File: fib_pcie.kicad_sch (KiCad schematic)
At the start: 59 parts, among them J901 Bus_M.2_2199230-6, J902 Bus_M.2_1-2199230-6, Y901 Oscillator_SMD_32.768kHz_ECS_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

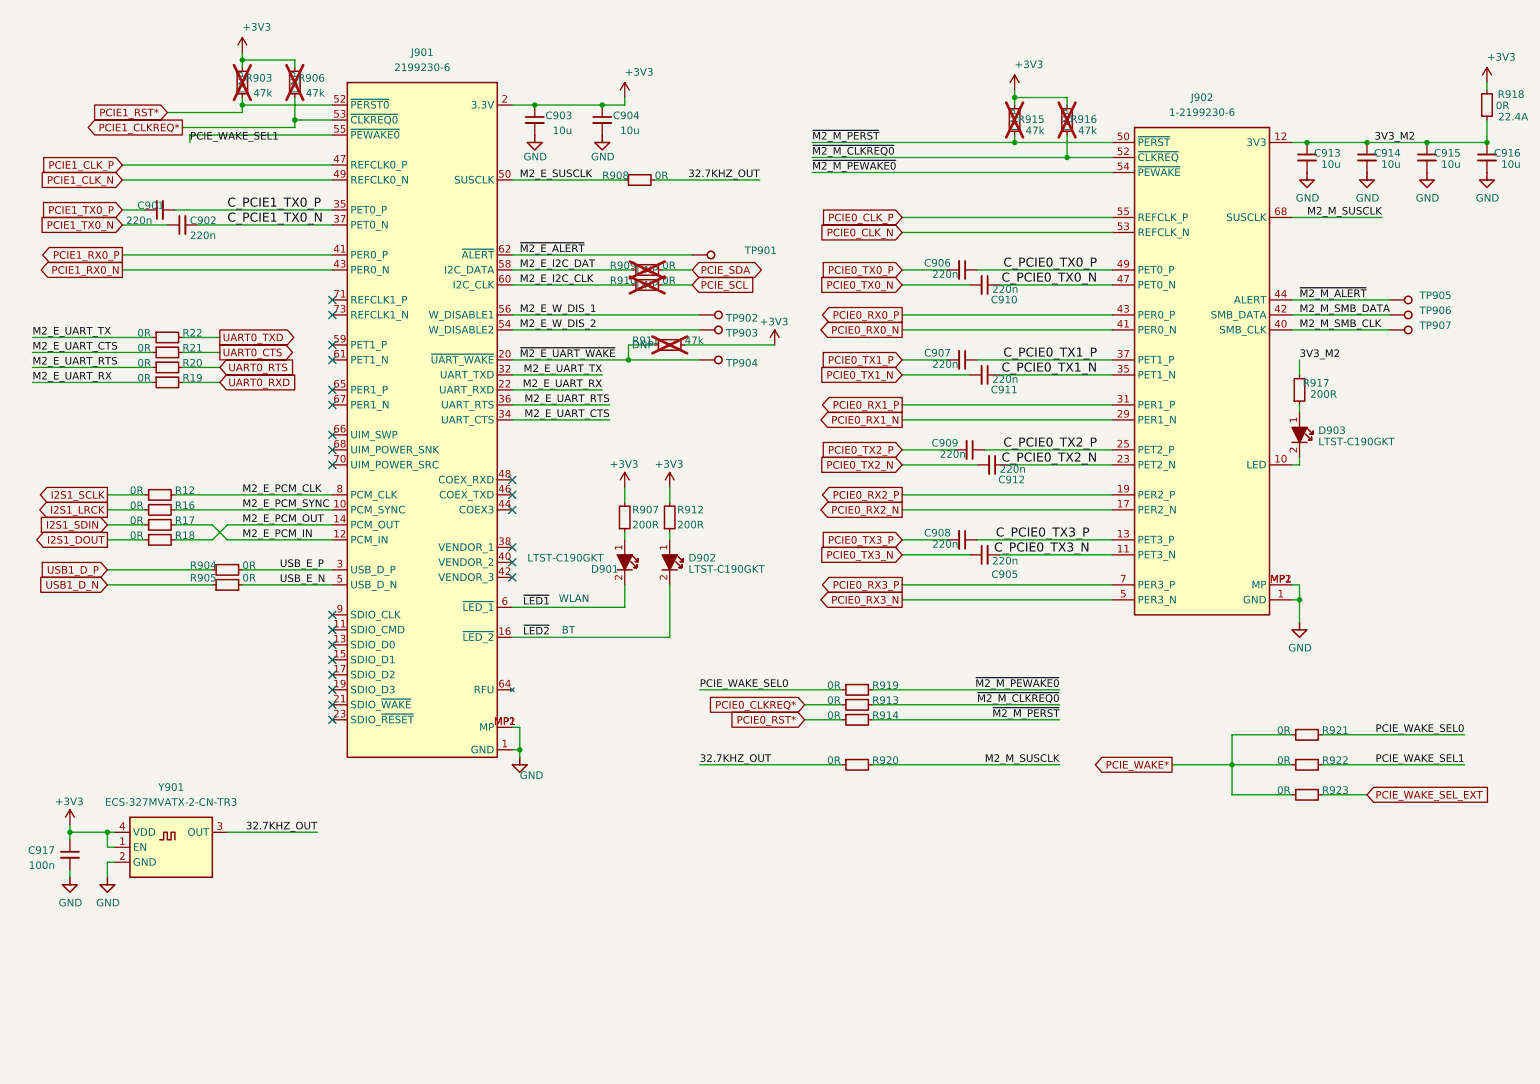
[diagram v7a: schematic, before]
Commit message: added all missing footprints, fixed library & footprint links, did layout out 99% of components, all that's left is rtc(?), peripherals, routing & lengthmatching and final sanity checks
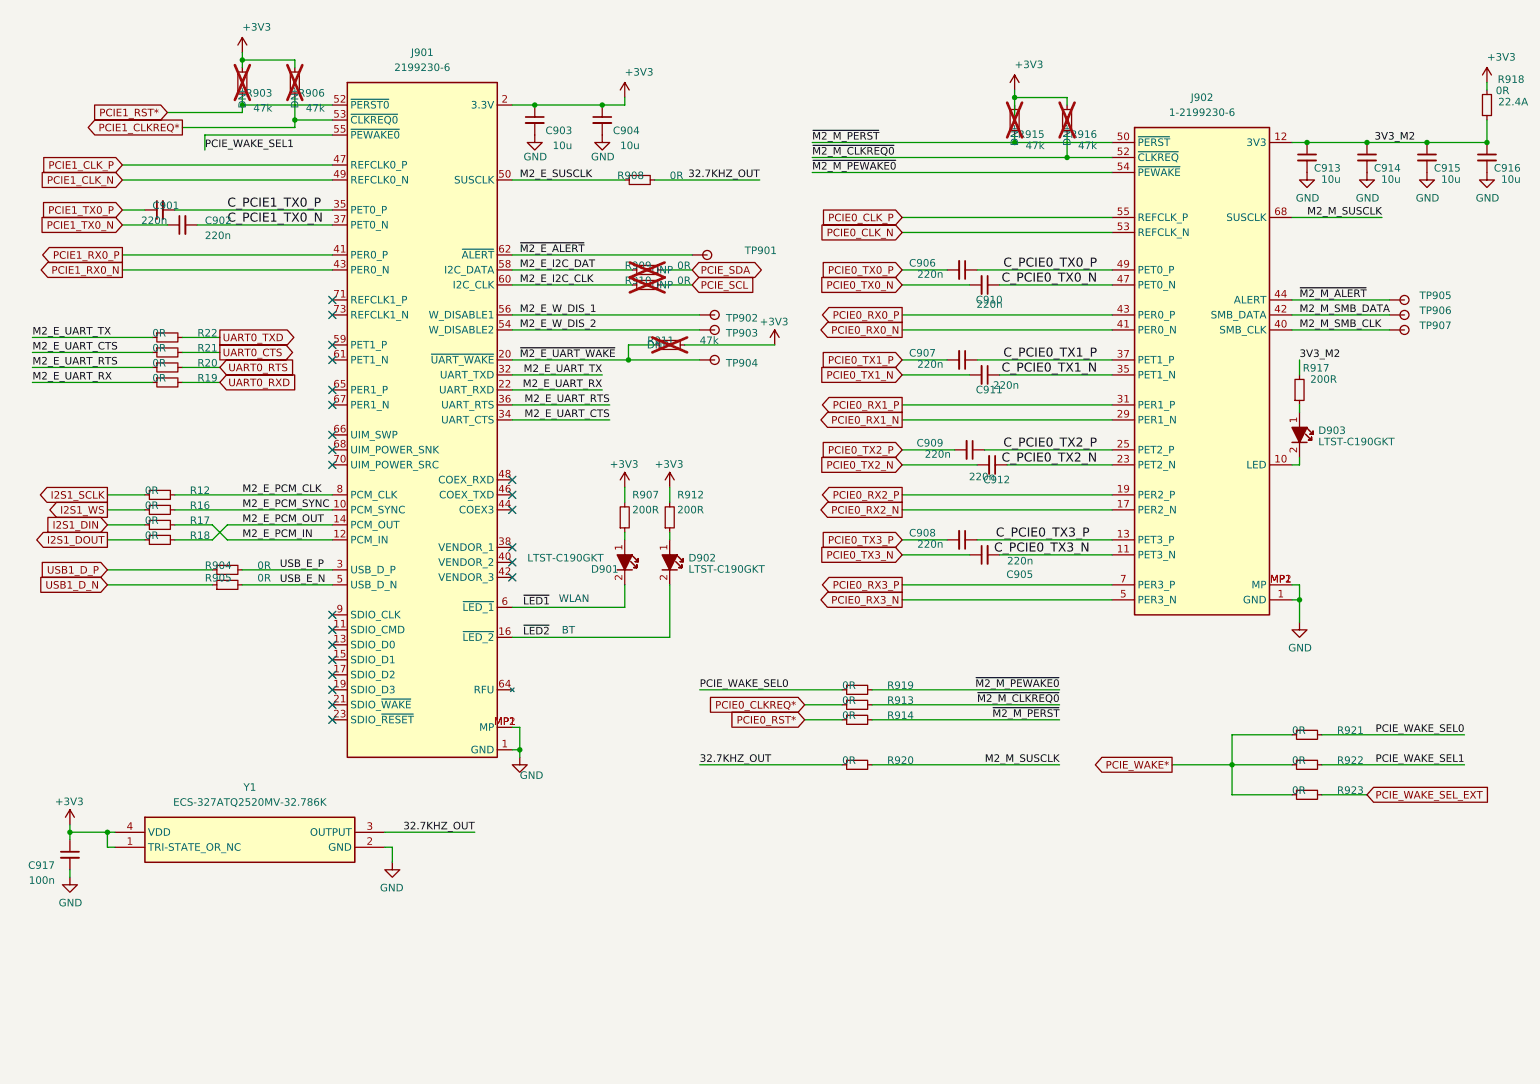
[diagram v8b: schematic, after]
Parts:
- removed Y901: Oscillator_SMD_32.768kHz_ECS_2520MV, jetson-orin-baseboard-footprints:Oscillator_SMD_ECS_2520MV_2.5x2mm, symbol jetson-orin-baseboard:Oscillator_32.768kHz_ECS_2520MV
- added Y1: ECS-327ATQ2520MV-32.786K, Fibel2:ECS2520MV, symbol Fibel2:ECS-327ATQ2520MV-32.786K
- C901, C902, C905, C906, C907, C908, C909, C910, C911, C912: symbol jetson-orin-baseboard:C_220n_0402 -> Fibel2:C_Small_Rota
- C903, C904, C913, C914, C915, C916: symbol jetson-orin-baseboard:C_10u_0603 -> Fibel2:C_Small_Rota
- C917: symbol jetson-orin-baseboard:C_100n_0402 -> Fibel2:C_Small_Rota
- D901, D902, D903: symbol jetson-orin-baseboard:LED_G_0603_LTST-C190GKT -> Fibel2:LED_G_0603_LTST-C190GKT
- R12, R16, R17, R18, R19, R20, R21, R22, R913, R914, R919, R920, R921, R922, R923: value R_0R_0402 -> R_Small_Rota; symbol jetson-orin-baseboard:R_0R_0402 -> Fibel2:R_Small_Rota
- R903, R906, R911, R915, R916: symbol jetson-orin-baseboard:R_47k_0402 -> Fibel2:R_Small_Rota
- R904, R905, R908, R909, R910: symbol jetson-orin-baseboard:R_0R_0402 -> Fibel2:R_Small_Rota
- R907, R912, R917: symbol jetson-orin-baseboard:R_200R_0402 -> Fibel2:R_Small_Rota
- R918: symbol jetson-orin-baseboard:R_0R_22.4A_0603 -> Fibel2:R_Small_Rota
- TP901, TP902, TP903, TP904, TP905, TP906, TP907: value TP_0.75mm_SMD -> TestPoint; symbol jetson-orin-baseboard:TP_0.75mm_SMD -> Fibel2:TestPoint
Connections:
- net +3V3: now also Y1.1 (TRI-STATE_OR_NC), Y1.4 (VDD); no longer R915.1
- net 32.7KHZ_OUT: now also Y1.3 (OUTPUT)
- net GND: now also Y1.2 (GND)
- net I2S1_LRCK renamed I2S1_WS
- net I2S1_SDIN renamed I2S1_DIN
